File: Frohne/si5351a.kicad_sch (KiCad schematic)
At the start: 9 parts, among them J8 BNC, U4 MS5351M

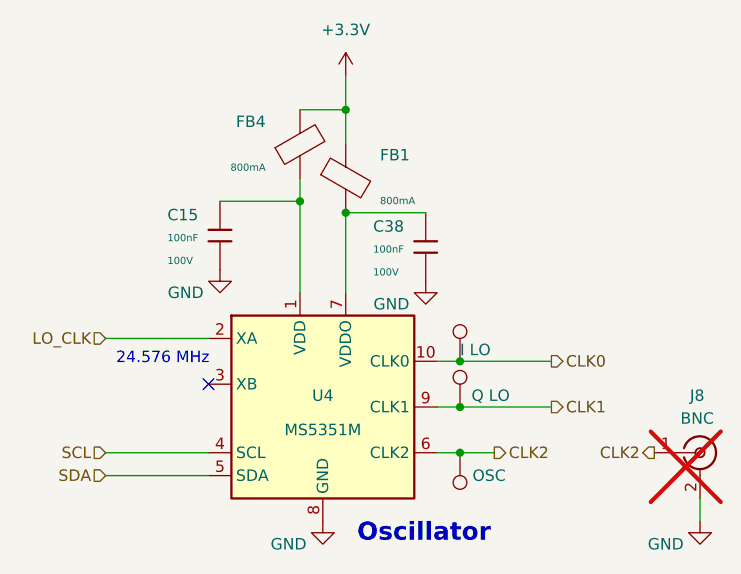
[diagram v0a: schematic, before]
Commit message: Tuned length of I and Q.
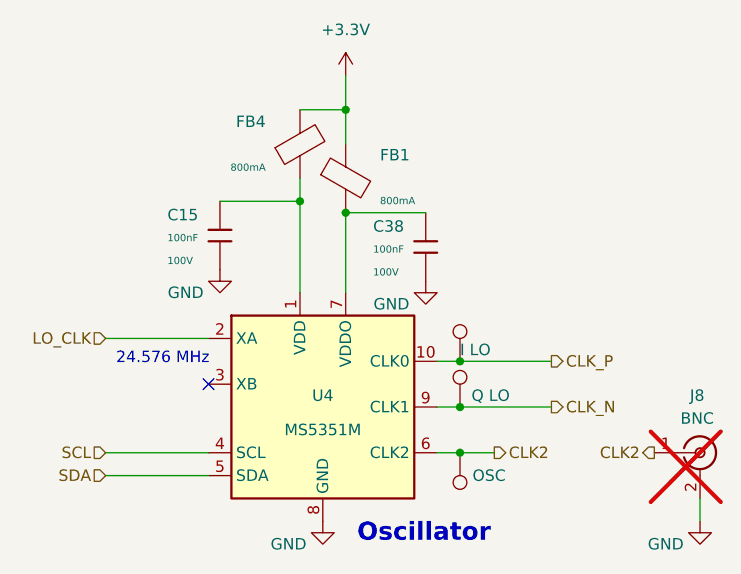
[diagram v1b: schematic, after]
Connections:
- net CLK0 renamed CLK_P
- net CLK1 renamed CLK_N
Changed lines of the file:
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@@
 		)
 	)
-	(hierarchical_label "CLK1"
+	(hierarchical_label "CLK_N"
 		(shape output)
 		(at 165.1 113.03 0)
@@
 		)
 	)
-	(hierarchical_label "CLK0"
+	(hierarchical_label "CLK_P"
 		(shape output)
 		(at 165.1 107.95 0)
